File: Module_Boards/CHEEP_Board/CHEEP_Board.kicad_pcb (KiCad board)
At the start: 6 copper layers, 17.5 x 26.4 mm, 53 parts, among them U2 HEEPocrates, U3 SIT1532AC-J5-DCC-32.768D, U4 W25Q128JWYIQ

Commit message: Big push. Fixed the issues that were pending. See github
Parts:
- removed C13: 100n 10V, X-MODs_PcbLib:C0402
- removed the G*** at (113.5, 114.6)
- removed the G*** at (101.5, 92.6)
- removed SW1: ~, X-MODs_PcbLib:TL1030AF160AQJ
- removed U1: ~, X-MODs_PcbLib:X2SON-6
- removed kibuzzard-67265B69: G***, kibuzzard-67265B69
- removed kibuzzard-67265C69: G***, kibuzzard-67265C69
- R1: value 100K -> 10K0
- moved C17 10.2 mm to (111.3, 109.0), turned to -90 degrees
- moved U7 8.68 mm to (110.2, 109.0), turned to -90 degrees
- moved R8 6.53 mm to (113.2, 109.0), turned to -90 degrees
- moved C16 5.31 mm to (113.2, 111.5), turned to -90 degrees
- moved R9 4.87 mm to (112.3, 109.0), turned to -90 degrees
- moved R5 4.75 mm to (106.5, 108.7), turned to 90 degrees
- moved R6 4.56 mm to (101.6, 108.7), turned to 90 degrees
- moved R1 4.37 mm to (102.8, 112.0)
- moved kibuzzard-67265A85 3.81 mm to (100.6, 95.2)
- moved kibuzzard-67265AAD 3.81 mm to (100.6, 100.4)
- moved kibuzzard-67265ADF 3.81 mm to (100.6, 106.1)
- moved kibuzzard-67265AFB 3.69 mm to (100.6, 111.1), turned to 90 degrees
- moved R7 3.61 mm to (106.5, 110.5), turned to -90 degrees
- moved R4 3.28 mm to (101.6, 110.5), turned to -90 degrees
- moved C15 2.82 mm to (104.8, 112.0), turned to 180 degrees
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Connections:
- J1 pad 1: VCORE -> JTAG_TDO
- J1 pad 10: PMIC_nRST -> FLASH_MISO
- J1 pad 11: SOC_RST_OUT -> FLASH_CS
- J1 pad 12: FLASH_MOSI -> FLASH_nWP
- J1 pad 13: FLASH_MISO -> FLASH_nHLD_nRST
- J1 pad 14: FLASH_CS -> FLASH_SCK
- J1 pad 15: FLASH_nWP -> I2C_SDA_HEEP
- J1 pad 16: FLASH_nHLD_nRST -> I2C_SCL_HEEP
- J1 pad 17: FLASH_SCK -> GND
- J1 pad 18: I2C_SDA_HEEP -> +1V8
- J1 pad 19: I2C_SCL_HEEP -> VCORE
- J1 pad 2: +1V8 -> JTAG_TDI
- J1 pad 20: +1V8 -> GND
- J1 pad 21: VCORE -> UART_RX_HEEP
- J1 pad 22: GND -> UART_TX_HEEP
- J1 pad 23: UART_RX_HEEP -> SPI_MOSI_HEEP
- J1 pad 24: UART_TX_HEEP -> SPI_MISO_HEEP
- J1 pad 25: SPI_MOSI_HEEP -> SPI_SD2_HEEP
- J1 pad 26: SPI_MISO_HEEP -> SPI_SD3_HEEP
- J1 pad 27: SPI_SD2_HEEP -> SPI_CS1_HEEP
- J1 pad 28: SPI_SD3_HEEP -> SPI_CS0_HEEP
- J1 pad 29: SPI_CS1_HEEP -> SPI_SCK_HEEP
- J1 pad 3: GND -> JTAG_TRST
- J1 pad 30: SPI_CS0_HEEP -> GND
- J1 pad 31: SPI_SCK_HEEP -> BOOT_SEL_EXT
- J1 pad 32: +1V8 -> GPIO_23
- J1 pad 33: VCORE -> GPIO_22
- J1 pad 34: GND -> GPIO_21
- J1 pad 35: BOOT_SEL_EXT -> GPIO_20
- J1 pad 36: GPIO_23 -> GPIO_19
- J1 pad 37: GPIO_22 -> GPIO_18
- J1 pad 38: GPIO_21 -> GPIO_17
- J1 pad 39: GPIO_20 -> GPIO_16
- J1 pad 4: JTAG_TDO -> JTAG_TMS
- J1 pad 40: GPIO_19 -> GPIO_15
- J1 pad 41: GPIO_18 -> GPIO_14
- J1 pad 42: GPIO_17 -> GPIO_13
- J1 pad 43: GPIO_16 -> GPIO_12
- J1 pad 44: GPIO_15 -> GPIO_11
- J1 pad 45: GPIO_14 -> GPIO_10
- J1 pad 46: GPIO_13 -> GPIO_9
- J1 pad 47: GPIO_12 -> VCORE
- J1 pad 48: GPIO_11 -> +1V8
- J1 pad 49: GPIO_10 -> GND
- J1 pad 5: JTAG_TDI -> JTAG_TCK
- J1 pad 50: GPIO_9 -> GPIO_8
- J1 pad 51: VCORE -> GPIO_7
- J1 pad 52: +1V8 -> GPIO_6
- J1 pad 53: GND -> GPIO_5
- J1 pad 54: GPIO_8 -> GPIO_4
- J1 pad 55: GPIO_7 -> GPIO_3
- J1 pad 56: GPIO_6 -> GPIO_2
- J1 pad 57: GPIO_5 -> GPIO_1
- J1 pad 58: GPIO_4 -> GPIO_0
- J1 pad 6: JTAG_TRST -> Manual_RST
- J1 pad 7: JTAG_TMS -> PMIC_nRST
- J1 pad 8: JTAG_TCK -> SOC_RST_OUT
- J1 pad 9: Manual_RST -> FLASH_MOSI
- R1 pad 1: BOOT_SEL_EXT -> +1V8
- R1 pad 2: GND -> BOOT_SEL_EXT
- U2 pad 86: /[1] HEEPocrates/BOOT_SELECT -> BOOT_SEL_EXT
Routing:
- net VCORE: track 83.4 -> 63.2 mm
- net /[2] Connectors & Flash/nSOC_RST: track 16.9 -> 4.75 mm
- net FLASH_SCK: track 20.0 -> 31.2 mm, vias 2 -> 1
- net SOC_RST_OUT: track 10.6 -> 20.4 mm, vias 1 -> 2
- net JTAG_TRST: track 33.0 -> 40.3 mm, vias 1 -> 2
- net /[1] HEEPocrates/BOOT_SELECT: track 7.13 -> 0.00 mm, vias 2 -> 0
- net PMIC_nRST: track 19.2 -> 26.3 mm
- net BOOT_SEL_EXT: track 19.8 -> 24.8 mm, vias 1 -> 3
- net I2C_SDA_HEEP: track 13.1 -> 8.96 mm
- net FLASH_CS: track 17.2 -> 21.2 mm, vias 2 -> 3
- net JTAG_TCK: track 5.80 -> 9.75 mm
- net Manual_RST: track 29.2 -> 25.3 mm
- net JTAG_TDI: track 7.60 -> 11.4 mm
- net I2C_SCL_HEEP: track 13.3 -> 9.57 mm
- net /[2] Connectors & Flash/RST_A: track 1.14 -> 4.85 mm
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- added copper zone on In3.Cu, net GND
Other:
- board size 17.5 x 26.4 mm -> 17.5 x 23.9 mm
- board text added: "B"

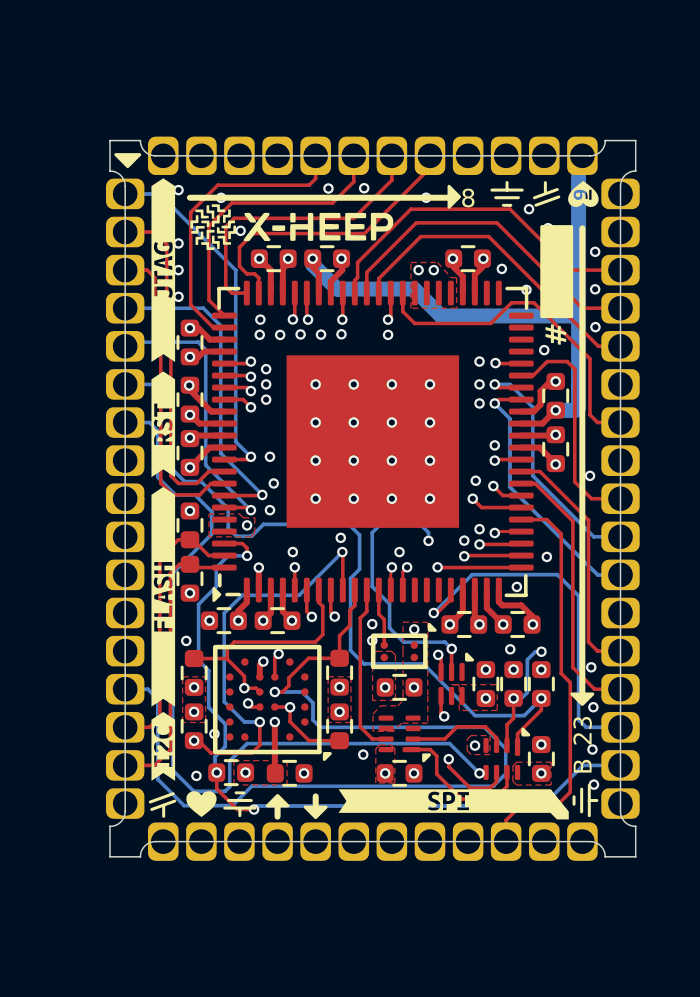
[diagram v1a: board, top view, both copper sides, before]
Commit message: Fixed bugs. Added comments. Push before changing the ADC
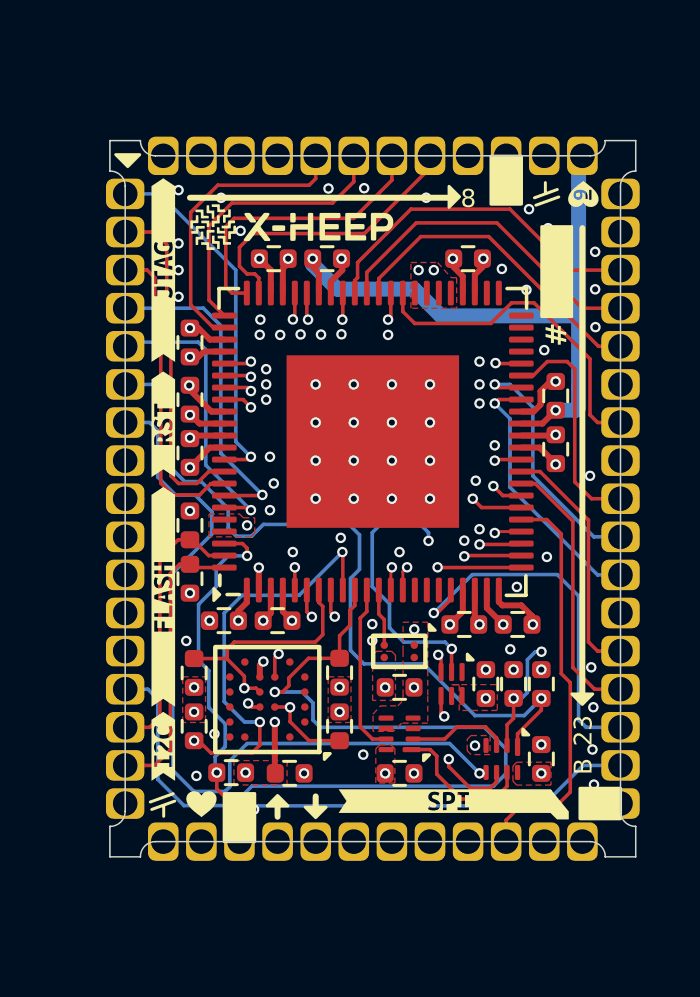
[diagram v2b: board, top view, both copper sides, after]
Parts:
- renumbered C14 to C13, C15 to C14, C16 to C15, C17 to C16, C18 to C17, U3 to OSC1, U2 to U1, U4 to U2, U5 to U3, U6 to U4, U7 to U5

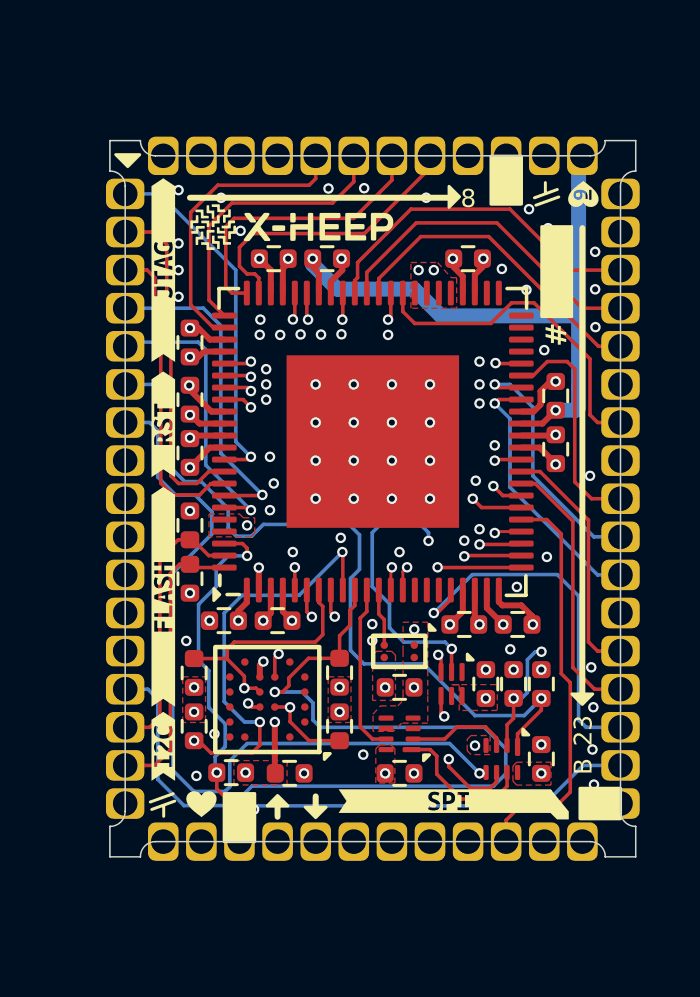
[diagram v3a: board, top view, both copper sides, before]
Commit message: Added fabrication panel. Now with latest designs
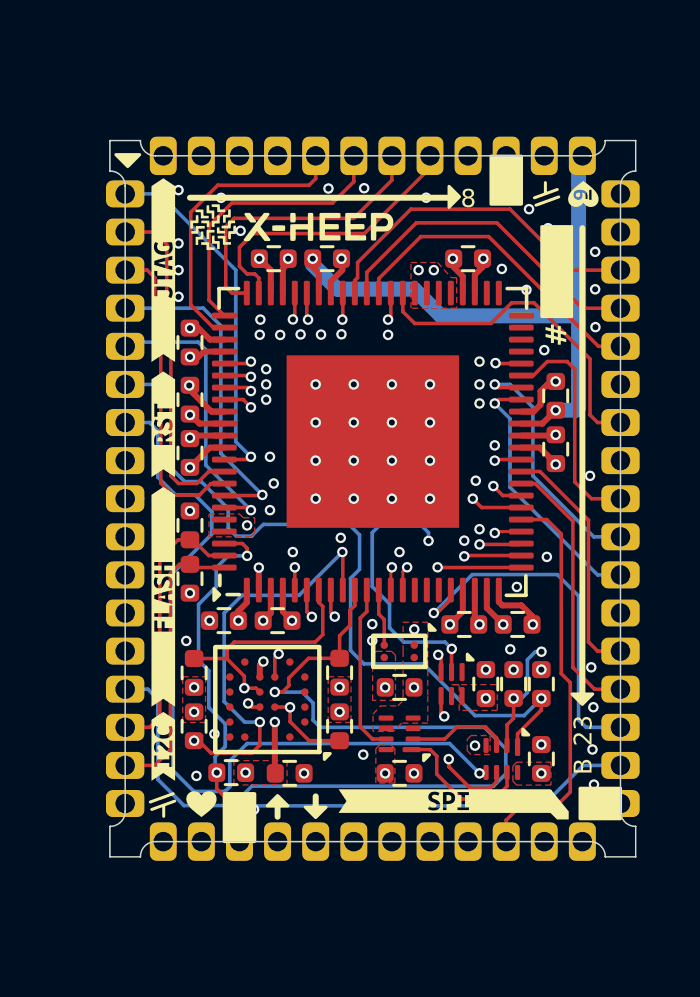
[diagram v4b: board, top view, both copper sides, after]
